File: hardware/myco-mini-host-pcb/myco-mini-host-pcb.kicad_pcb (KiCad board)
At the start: 2 copper layers, 53.5 x 138.4 mm, 27 parts, among them J1 Conn_01x17_Female, J2 Conn_01x17_Female, Q1 AO3401A, Q2 AO3401A, SW1 EM-04-Q, U1 XC9145B33CMR-G, U2 SHT41-AD1B-R2, U3 BH1750FVI-TR

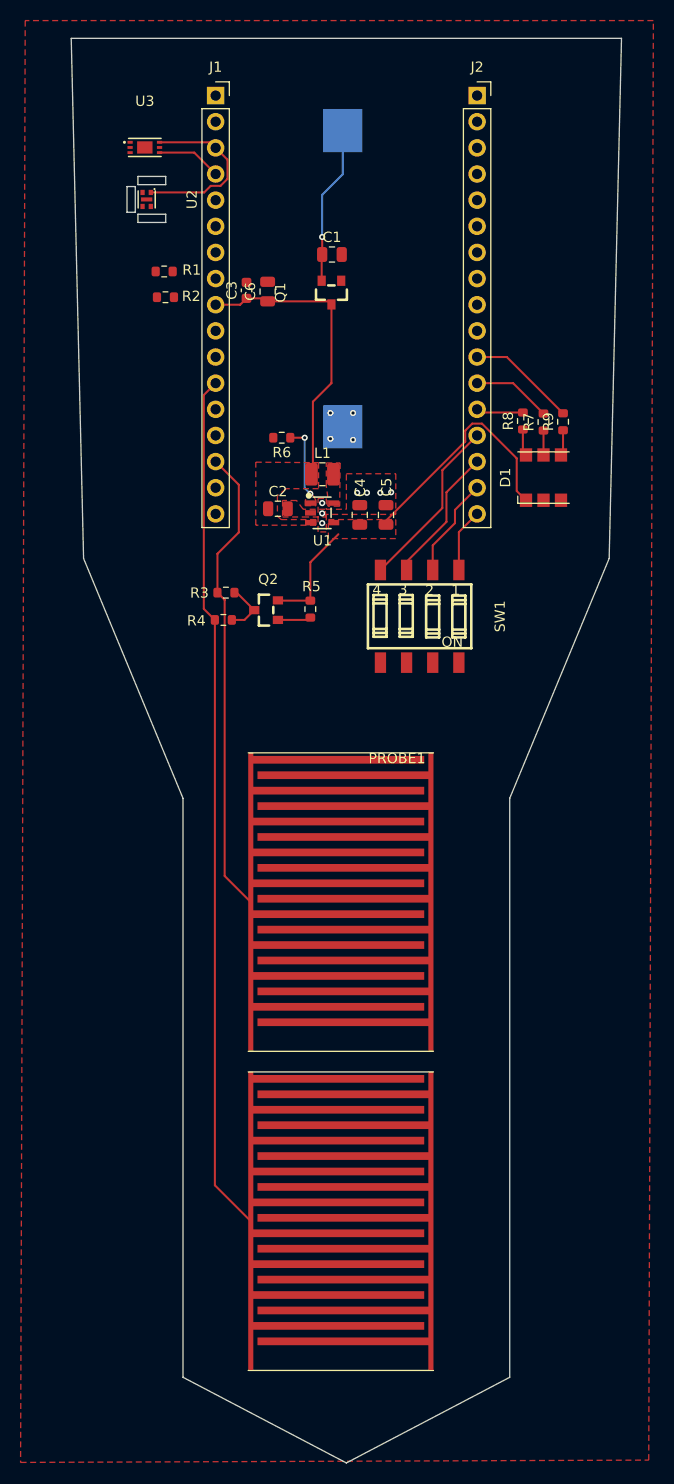
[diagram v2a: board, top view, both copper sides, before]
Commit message: chore: sync PCB apres passe manuelle utilisateur (placement/routage), capture gen_pcb.py
Contour de carte et decoupe thermique U2 affines a la main (coins arrondis),
remap GPIO D1/R7-R9 vers J2 et I2C vers J1 avec vrai routage cuivre (SDA sur
F.Cu, SCL via via + B.Cu pour eviter le croisement des deux nets). gen_pcb.py
mis a jour en lecture seule pour refleter l'etat courant (placement, contour
polygonal, geometrie de la decoupe U2) - fichier live non touche.

Co-Authored-By: Claude Sonnet 5 <noreply@anthropic.com>
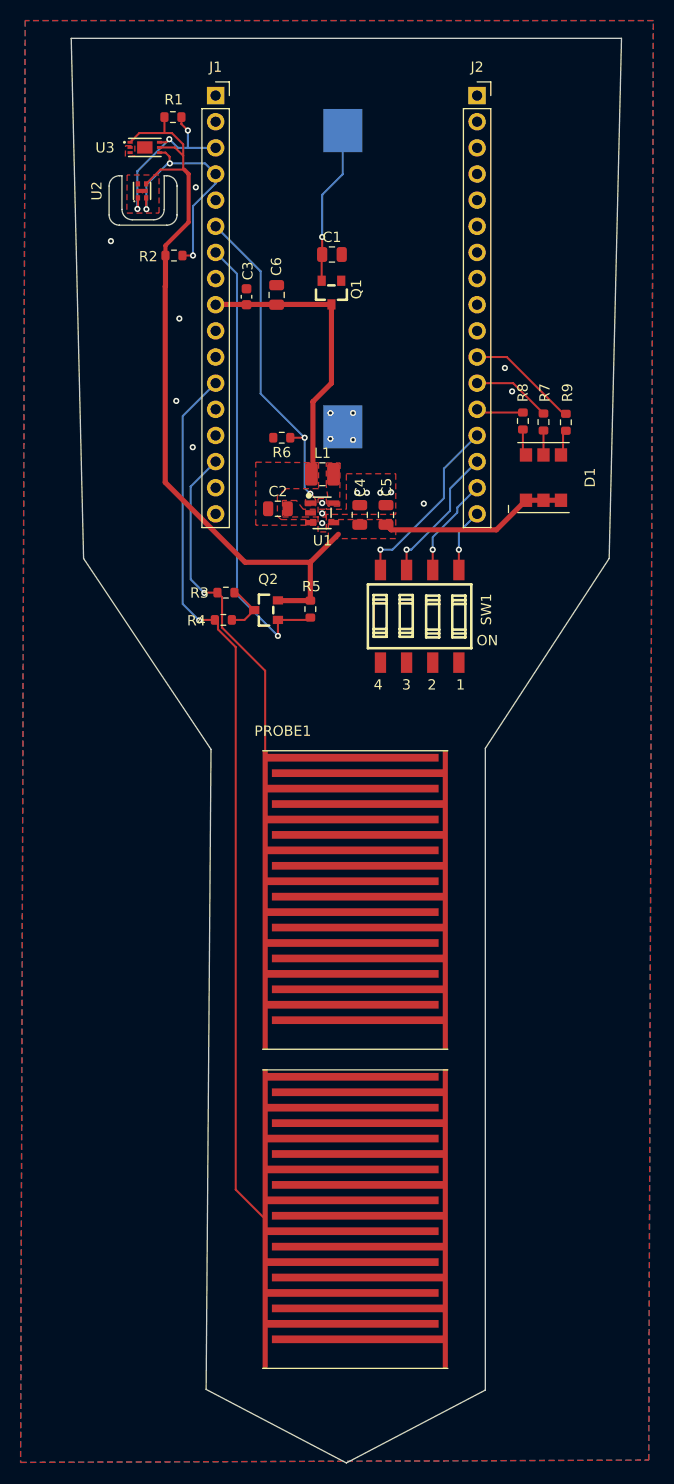
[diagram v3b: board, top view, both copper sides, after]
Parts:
- U2: value SHT41-AD1B-R2 -> SHT41
- U3: value BH1750FVI-TR -> BH1750
- moved R1 15.0 mm to (60.9, 28.1), turned to 0 degrees
- moved R2 4.13 mm to (61.0, 41.6), turned to 0 degrees
- moved PROBE1 1.41 mm to (69.6, 89.7)
- moved U2 0.94 mm to (57.9, 35.3), turned to 90 degrees
- moved C6 0.94 mm to (71.0, 45.4)
- moved C3 0.62 mm to (68.0, 45.6)
- moved R9 0.28 mm to (99.1, 57.8)
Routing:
- net /VOUT_3V3: track 34.2 -> 94.8 mm
- net /P1_14_SOIL_SW: track 3.24 -> 44.5 mm, vias 0 -> 1
- net /P1_13_BOOST_EN: track 7.08 -> 31.2 mm
- net /P1_11_SCL: track 6.40 -> 23.1 mm, vias 0 -> 3
- net /P1_04_SOIL_ADC2: track 83.8 -> 86.8 mm, vias 0 -> 1
- net /P1_07_SOIL_ADC1: track 45.9 -> 47.4 mm, vias 0 -> 1
- net /P1_10_SDA: track 17.2 -> 18.3 mm, vias 0 -> 3
- net /VDD_NRF: track 30.4 -> 29.4 mm
- net /P2_03_DIP3: track 17.0 -> 17.6 mm, vias 0 -> 1
- net /P2_02_DIP2: track 13.4 -> 13.6 mm, vias 0 -> 1
- net GND: track 0.00 -> 0.09 mm, vias 11 -> 18
- net /P2_01_DIP1: vias 0 -> 1
- net /P2_00_DIP0: vias 0 -> 1
- net (no net): vias 0 -> 1
- added copper zone on B.Cu, net GND
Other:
- outline, holes or cut-outs redrawn

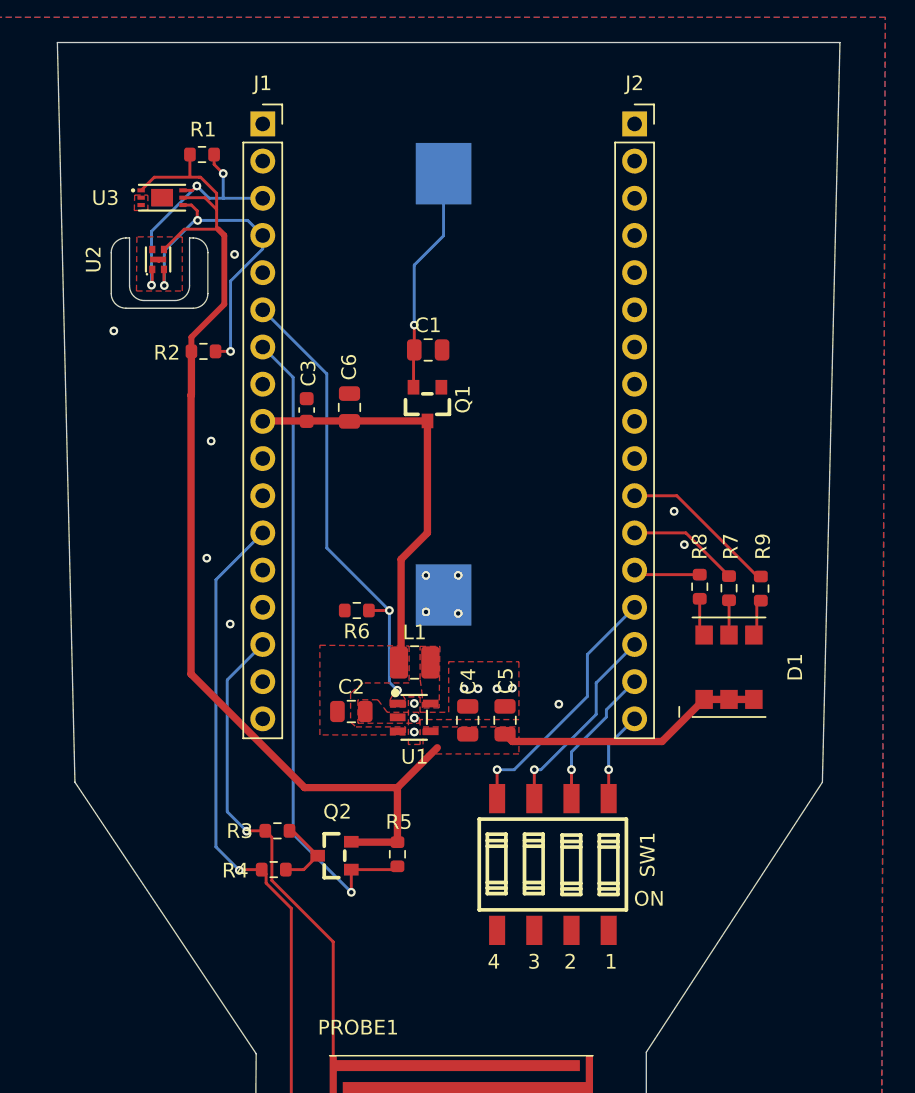
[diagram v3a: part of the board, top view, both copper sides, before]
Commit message: feat: protection backfeed (U4/MAX40203), rail nRF54 sur boost, remap GPIO
- U4 (MAX40203AUK+T): diode ideale entre Q1 et VDD_NRF, bloque le
  backfeed depuis le probe SWD (breakout J5) vers la CR2032 - remplace
  la premiere tentative LM66100 (rejetee apres verification, seuil
  RCB trop insensible pour nos courants)
- SW1: EM-04-Q remplace par DM-04-V (rupture de stock LCSC), meme
  pairing electrique, footprint tourne 90deg
- Bouton reset SW2 (TS-1187A-B-A-B) + R10 series sur NRESET (J2 pin1)
- Fix SDA/SCL inverses sur U3 (BH1750) - bug trouve par audit, U3.4
  et U3.6 etaient sur les mauvais nets
- Architecture alim revue : le nRF54 (J1 pin9) passe de VDD_NRF (pile
  directe) a VOUT_3V3 (boost, toujours actif) pour eliminer le
  depassement d'abs-max GPIO (VDD+0.3V) cause par les pull-ups
  VOUT_3V3 sur des pins references a VDD_NRF qui sague avec la pile
  - Q3 (AO3401A) : nouveau switch VOUT_3V3->SENSOR_3V3, alimente
    SHT41+BH1750+leurs pull-ups I2C (R1/R2), coupable independamment
  - Q4 (AO3401A) + R11/R12 (diviseur 1M/1M) : mesure batterie via
    BAT_RAW, switchee pour eviter la fuite continue (remplace le
    canal SAADC interne VDD, plus valide une fois VDD_NRF regule)
  - Q3/Q4 partagent un seul GPIO de controle (P1_12_SENSOR_EN)
- Remap GPIO pour faciliter le routage : BOOST_EN P1.13->P1.05,
  BAT_SENSE P1.05->P1.13, SOIL_SW P1.14->P1.08 (tous verifies
  General Purpose I/O dans la datasheet nRF54L15, P1.13 confirme
  AIN6 pour le besoin SAADC de BAT_SENSE)
- BOM et librairie (symboles/footprints/modeles 3D) mis a jour

Co-Authored-By: Claude Sonnet 5 <noreply@anthropic.com>
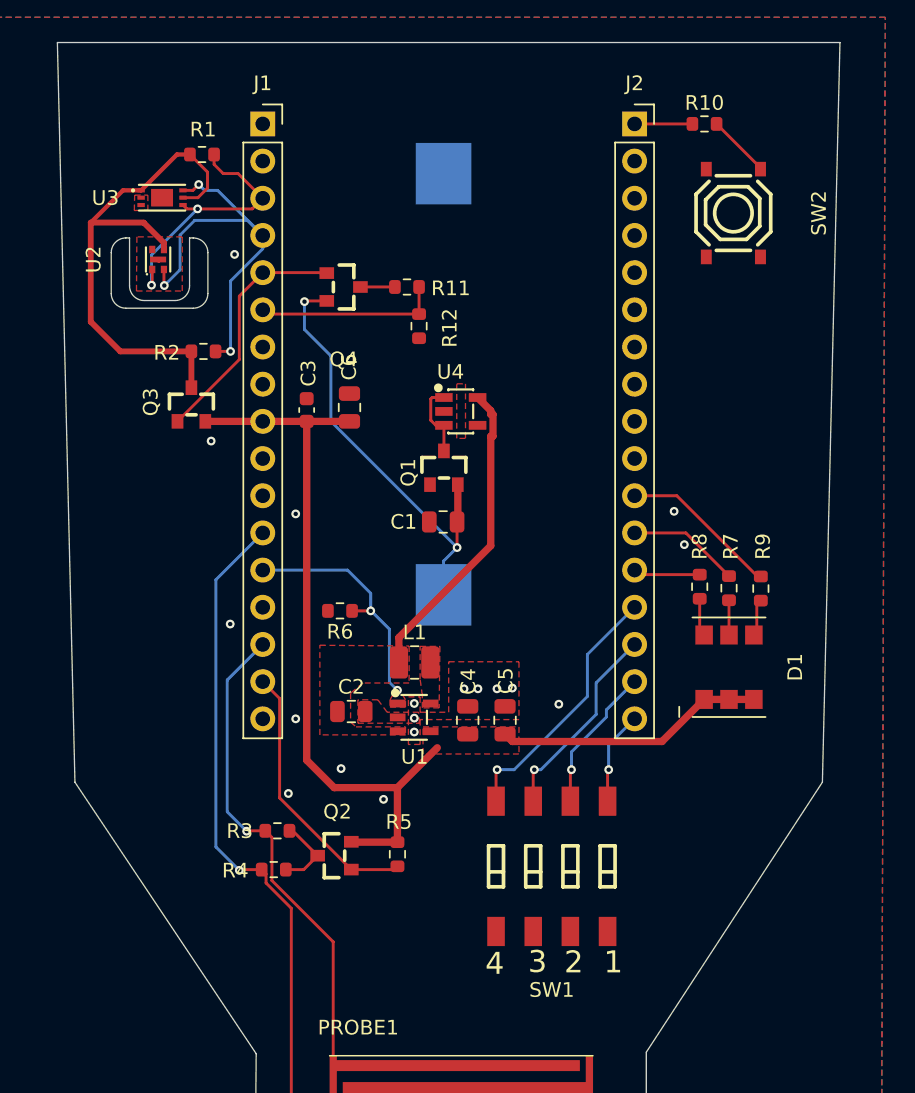
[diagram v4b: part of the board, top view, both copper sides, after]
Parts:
- added Q3: AO3401A, myco_host:SOT-23_L2.9-W1.3-P1.90-LS2.4-BR, F.Cu at (60.2, 45.2)
- added Q4: AO3401A, myco_host:SOT-23_L2.9-W1.3-P1.90-LS2.4-BR, F.Cu at (70.6, 37.2)
- added R10: 220, Resistor_SMD:R_0603_1608Metric, F.Cu at (95.2, 26.1)
- added R11: 1M, Resistor_SMD:R_0603_1608Metric, F.Cu at (74.9, 37.2)
- added R12: 1M, Resistor_SMD:R_0603_1608Metric, F.Cu at (75.7, 39.9)
- added SW2: TS-1187A-B-A-B, myco_host:SW-SMD_4P-L5.1-W5.1-P3.70-LS6.5-TL_H1.5, F.Cu at (97.2, 32.1)
- added U4: MAX40203AUK+T, myco_host:SOT-23-5_L3.0-W1.6-P0.95-LS2.8-BR, F.Cu at (78.6, 45.7)
- SW1: value EM-04-Q -> DM-04-V; footprint myco_host:SW-SMD_8P-L10.1-W6.0-P2.54-LS9.8 -> myco_host:SW-SMD_8P-L11.1-W6.2-P2.54-LS9.8
- U2: value SHT41 -> SHT41-AD1B-R2
- U3: value BH1750 -> BH1750FVI-TR
- moved C1 11.8 mm to (77.4, 53.2), turned to 180 degrees
- moved Q1 4.49 mm to (77.4, 49.5), turned to -90 degrees
- moved R6 1.15 mm to (70.3, 59.3)
- moved SW1 0.15 mm to (84.8, 76.8), turned to 180 degrees
- turned BT1 to -90 degrees
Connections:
- C3 pad 1: /VDD_NRF -> /VOUT_3V3
- C6 pad 1: /VDD_NRF -> /VOUT_3V3
- J1 pad 13: unconnected-(J1-Pin_13-Pad13) -> /P1_05_BOOST_EN
- J1 pad 16: unconnected-(J1-Pin_16-Pad16) -> /P1_08_SOIL_SW
- J1 pad 5: unconnected-(J1-Pin_5-Pad5) -> /P1_12_SENSOR_EN
- J1 pad 6: /P1_13_BOOST_EN -> /P1_13_BAT_SENSE
- J1 pad 7: /P1_14_SOIL_SW -> unconnected-(J1-Pin_7-Pad7)
- J1 pad 9: /VDD_NRF -> /VOUT_3V3
- J2 pad 1: unconnected-(J2-Pin_1-Pad1) -> /NRESET
- Q1 pad 3: /VDD_NRF -> /VDD_PROT
- Q2 pad 1: /P1_14_SOIL_SW -> /P1_08_SOIL_SW
- R1 pad 1: /VOUT_3V3 -> /SENSOR_3V3
- R2 pad 1: /VOUT_3V3 -> /SENSOR_3V3
- R5 pad 2: /P1_14_SOIL_SW -> /P1_08_SOIL_SW
- R6 pad 1: /P1_13_BOOST_EN -> /P1_05_BOOST_EN
- U1 pad 1: /P1_13_BOOST_EN -> /P1_05_BOOST_EN
- U2 pad 3: /VOUT_3V3 -> /SENSOR_3V3
- U3 pad 1: /VOUT_3V3 -> /SENSOR_3V3
- U3 pad 4: /P1_11_SCL -> /P1_10_SDA
- U3 pad 5: /VOUT_3V3 -> /SENSOR_3V3
- U3 pad 6: /P1_10_SDA -> /P1_11_SCL
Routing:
- net /P1_14_SOIL_SW: track 44.5 -> 0.00 mm, vias 1 -> 0
- net /SENSOR_3V3: track 0.00 -> 36.4 mm
- net /P1_13_BOOST_EN: track 31.2 -> 0.00 mm, vias 2 -> 0
- net /VOUT_3V3: track 94.8 -> 69.2 mm
- net /P1_08_SOIL_SW: track 0.00 -> 18.6 mm
- net /P1_12_SENSOR_EN: track 0.00 -> 17.0 mm
- net /P1_05_BOOST_EN: track 0.00 -> 16.7 mm, vias 0 -> 2
- net /BAT_RAW: track 15.4 -> 30.5 mm, vias 1 -> 2
- net /P1_13_BAT_SENSE: track 0.00 -> 12.6 mm
- net /VDD_NRF: track 29.4 -> 21.4 mm
- net /P1_11_SCL: track 23.1 -> 28.3 mm
- net /VDD_PROT: track 0.00 -> 5.19 mm
- net Net-(SW2-A): track 0.00 -> 4.33 mm
- net /NRESET: track 0.00 -> 3.95 mm
- net /BAT_SENSE_TOP: track 0.00 -> 2.36 mm
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- added copper zone on F.Cu, net /P1_05_BOOST_EN
- removed copper zone on F.Cu, net /P1_13_BOOST_EN

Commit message: fix: boost toujours actif (CE->VDD_NRF), modeles 3D, regles JLCPCB
- CE du XC9145 cable en dur sur VDD_NRF au lieu d'une GPIO : le boost
  alimente maintenant le nRF54 lui-meme, plus aucun scenario ou le
  firmware voudrait legitimement le couper (couperait sa propre
  alim) - supprime aussi le risque de brick si cette GPIO avait ete
  mise a l'etat bas par erreur
- R6 (pull-down CE) retire, plus necessaire - le tie direct satisfait
  deja l'exigence datasheet "ne pas laisser CE flottant"
- P1.05 redevient libre (broche J1 pin13)
- fix regression : label C2 revenu sur VDD_NRF au lieu de VOUT_3V3
  entre deux etapes precedentes (cause non identifiee avec certitude,
  isole aux 8 autres renommages de la meme tache qui etaient intacts)
- chemins de modeles 3D corriges sur les 8 footprints custom
  (${KIPRJMOD}/libs/... au lieu d'un chemin absolu casse)
- modeles 3D ajoutes pour U1 (XC9145, generique SOT-23-5 - LCSC n'a
  aucun modele pour ce package) et D1 (LED RGB 5050-6, meme raison)
- regles de conception resserrees pour matcher les minimums JLCPCB
  (min_clearance, min_via_diameter, min_via_annular_width,
  min_hole_to_hole) - geometrie actuelle du board deja conforme,
  DRC toujours propre apres resserrement
- placement/routage PCB (travail manuel utilisateur)

Co-Authored-By: Claude Sonnet 5 <noreply@anthropic.com>
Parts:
- removed R6: 100k, Resistor_SMD:R_0603_1608Metric
- moved U4 12.6 mm to (75.7, 58.0), turned to 0 degrees
- moved R12 7.72 mm to (70.6, 34.1), turned to 180 degrees
- moved R3 6.60 mm to (68.7, 80.4), turned to -90 degrees
- moved Q1 4.59 mm to (76.8, 54.1), turned to 90 degrees
- moved R4 3.42 mm to (66.2, 80.4), turned to -90 degrees
- moved C1 2.90 mm to (76.8, 50.4), turned to 0 degrees
- moved R11 1.13 mm to (74.1, 36.4), turned to 90 degrees
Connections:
- J1 pad 13: /P1_05_BOOST_EN -> unconnected-(J1-Pin_13-Pad13)
- U1 pad 1: /P1_05_BOOST_EN -> /VDD_NRF
- U2 pad 5: GND -> (no net)
- U3 pad 7: GND -> (no net)
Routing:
- net /P1_05_BOOST_EN: track 16.7 -> 0.00 mm, vias 2 -> 0
- net /VDD_NRF: track 21.4 -> 6.85 mm
- net /P1_13_BAT_SENSE: track 12.6 -> 16.6 mm, vias 0 -> 2
- net /SOIL_VCC: track 5.20 -> 7.14 mm
- net /VDD_PROT: track 5.19 -> 6.96 mm
- net /BAT_RAW: track 30.5 -> 28.8 mm, vias 2 -> 1
- net /P1_07_SOIL_ADC1: track 47.4 -> 48.8 mm
- net /P2_06_LED_B: track 10.6 -> 11.7 mm
- net /P2_05_LED_G: track 7.67 -> 8.64 mm
- removed copper zone on F.Cu, net /P1_05_BOOST_EN

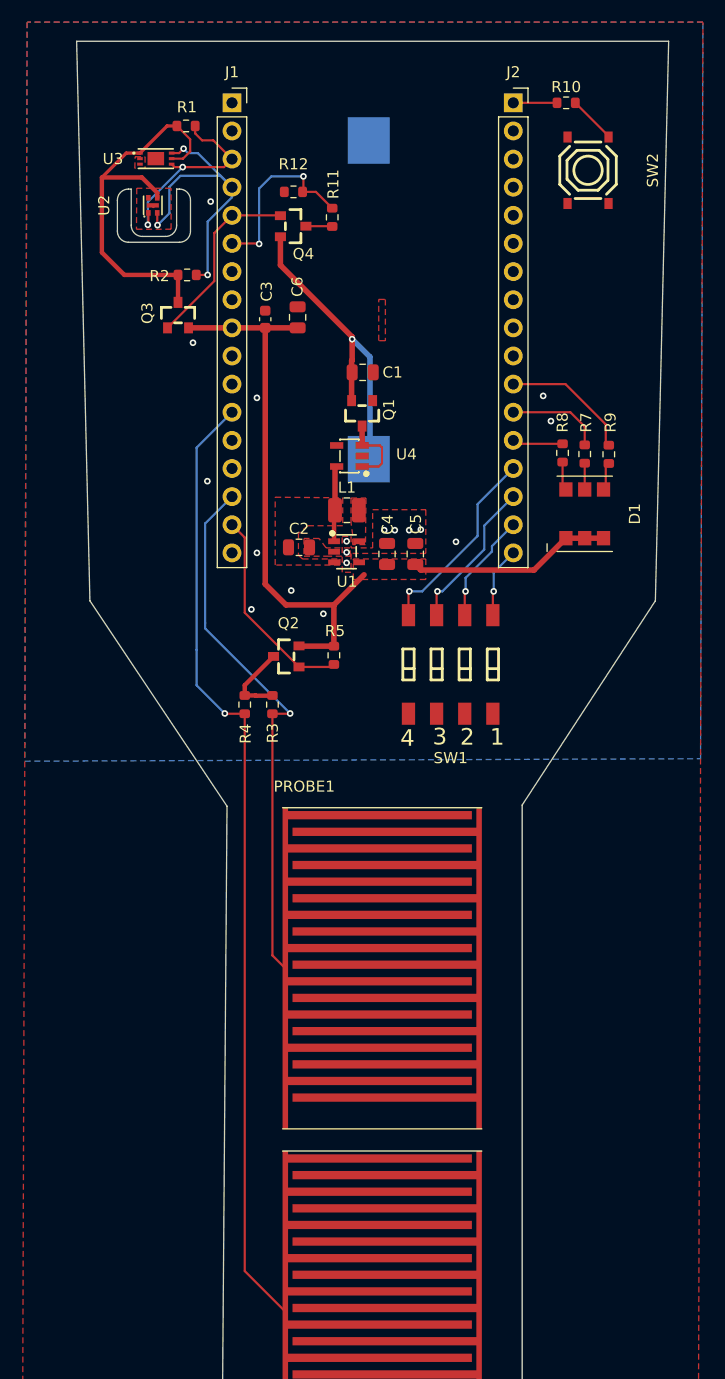
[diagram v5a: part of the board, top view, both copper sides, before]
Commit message: chore: snapshot avant corrections audit #2 (passe manuelle utilisateur)
Etat du schema et du PCB apres la passe manuelle de l'utilisateur
(alignement des textes/labels pour qu'ils ne chevauchent plus les
symboles, placement/routage PCB), avant d'appliquer les corrections
remontees par le second audit Opus 5.

Point de retour propre pour les corrections a venir :
- Q1 (protection inversion polarite) oriente a l'envers
- pas de decouplage sur SENSOR_3V3
- pas de pull-up sur P1_12_SENSOR_EN (Q3/Q4 flottants au boot)
- LED rouge/vert croisees, stubs I2C orphelins
- BOM obsolete (R6 fantome, commentaire R11/R12)
- VDD_NRF mal nomme (n'alimente plus le nRF54)

Co-Authored-By: Claude Sonnet 5 <noreply@anthropic.com>
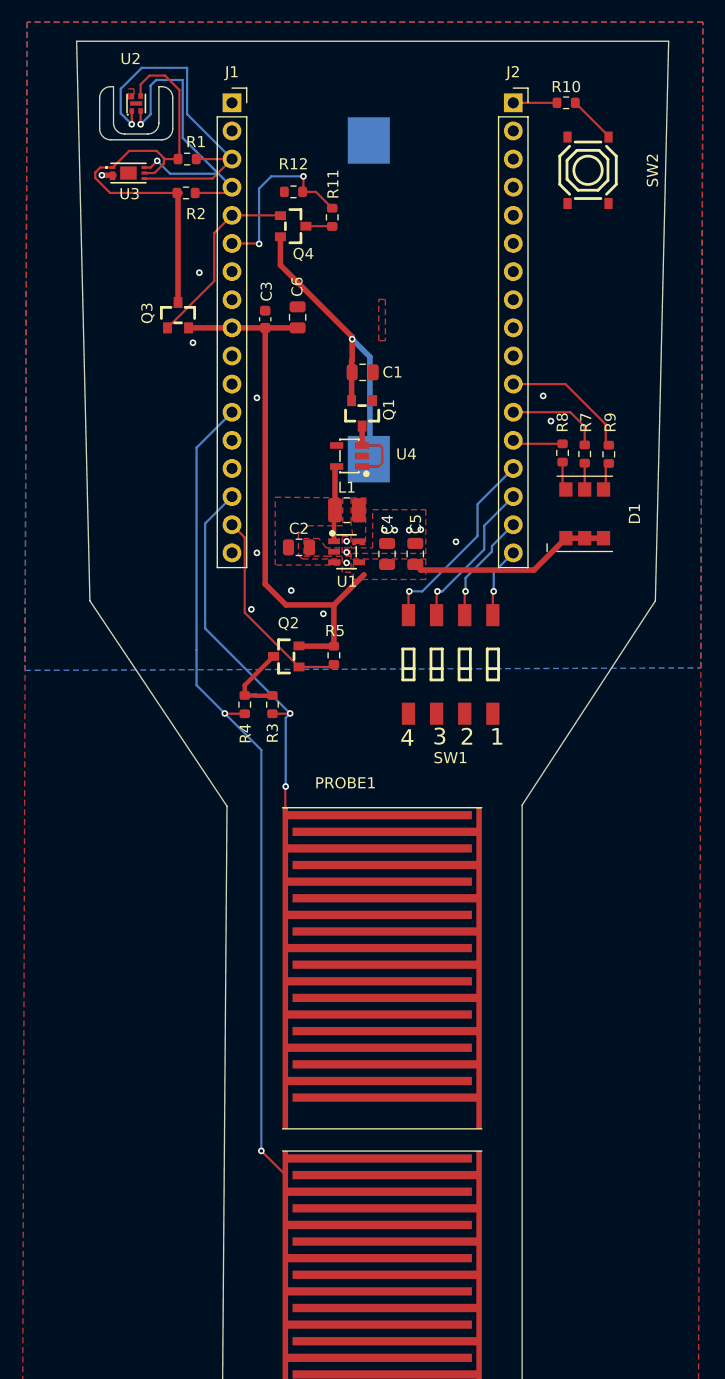
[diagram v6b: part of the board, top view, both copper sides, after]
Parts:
- moved U2 9.32 mm to (56.4, 26.1)
- moved R2 7.40 mm to (60.9, 34.2)
- moved R1 2.99 mm to (61.0, 31.1)
- moved U3 2.79 mm to (55.7, 32.4)
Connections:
- net /LED_B_NODE renamed Net-(D1-B)
- net /LED_G_NODE renamed Net-(D1-G)
- net /LED_R_NODE renamed Net-(D1-R)
- U2 pad 5: (no net) -> GND
- U3 pad 7: (no net) -> GND
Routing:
- net /P1_10_SDA: track 18.4 -> 33.4 mm, vias 2 -> 1
- net /SENSOR_3V3: track 36.4 -> 40.9 mm
- net /P1_11_SCL: track 28.3 -> 30.4 mm, vias 3 -> 2
- net GND: track 0.09 -> 1.38 mm, vias 17 -> 18
- net /P1_04_SOIL_ADC2: track 86.9 -> 85.6 mm, vias 1 -> 2
- net /P1_07_SOIL_ADC1: track 48.8 -> 48.6 mm, vias 1 -> 2
- net (no net): vias 1 -> 0
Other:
- outline, holes or cut-outs redrawn
